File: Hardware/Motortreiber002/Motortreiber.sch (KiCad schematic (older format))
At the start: 17 parts, among them J2 Screw_Terminal_01x04, J3 Screw_Terminal_01x04, U1 DRV8823

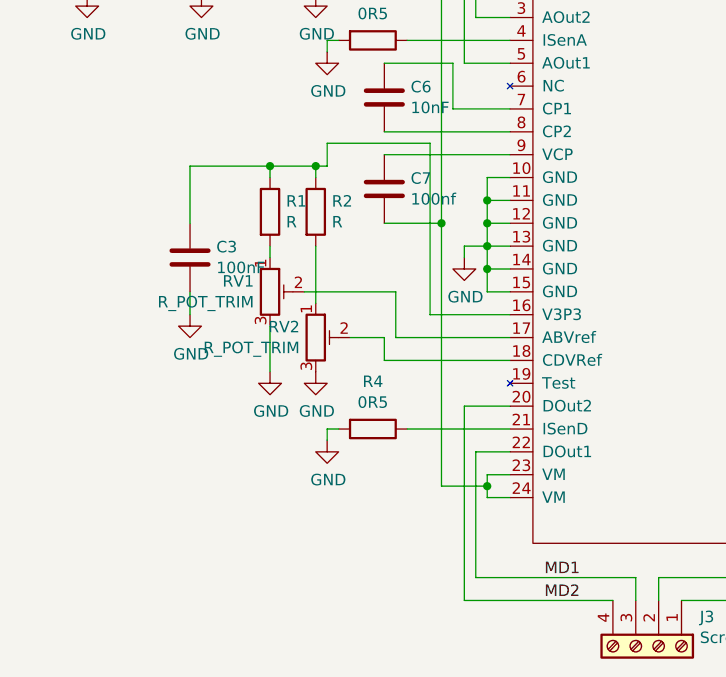
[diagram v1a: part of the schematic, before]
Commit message: 16 Motortreiber 1 ATXMega 128 mit USB USB Anschluss noch nicht fertig
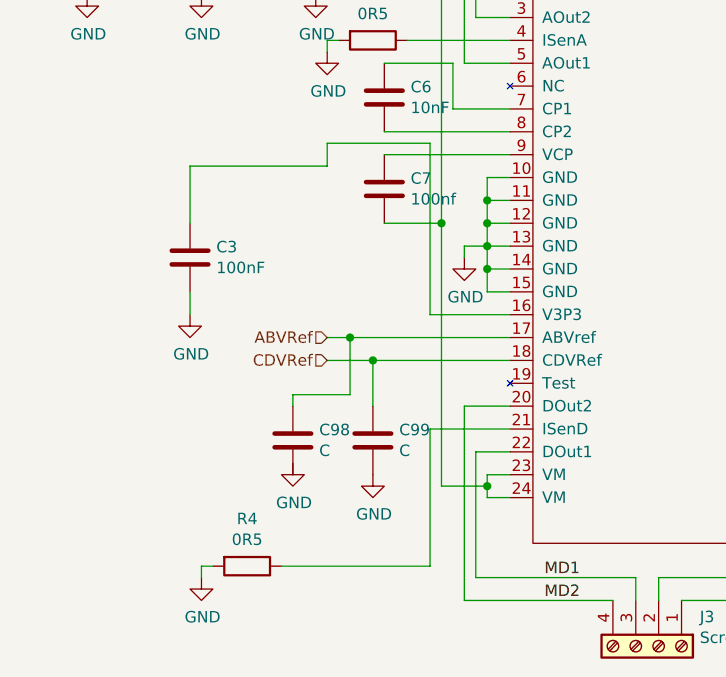
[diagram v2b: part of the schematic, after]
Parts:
- removed R1, R2: R, Resistor_SMD:R_0805_2012Metric_Pad1.15x1.40mm_HandSolder, symbol Device:R
- removed RV1, RV2: R_POT_TRIM, Potentiometer_THT:Potentiometer_Vishay_43_Horizontal, symbol Device:R_POT_TRIM
- added C98, C99: C, symbol Device:C
- renumbered C2 to C20, C3 to C21, C4 to C22, C5 to C23, C6 to C24, C7 to C25, J2 to J8, J3 to J9, R3 to R21, R4 to R22, R5 to R23, R6 to R24, U1 to U4
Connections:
- net GND: now also C99.2
- net ABVRef: now reaches U4.17 (ABVref)
- net ABVRef: now also C98.1
- net CDVRef: now reaches U4.18 (CDVRef)
- net CDVRef: now also C99.1
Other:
- moved on the sheet: R4

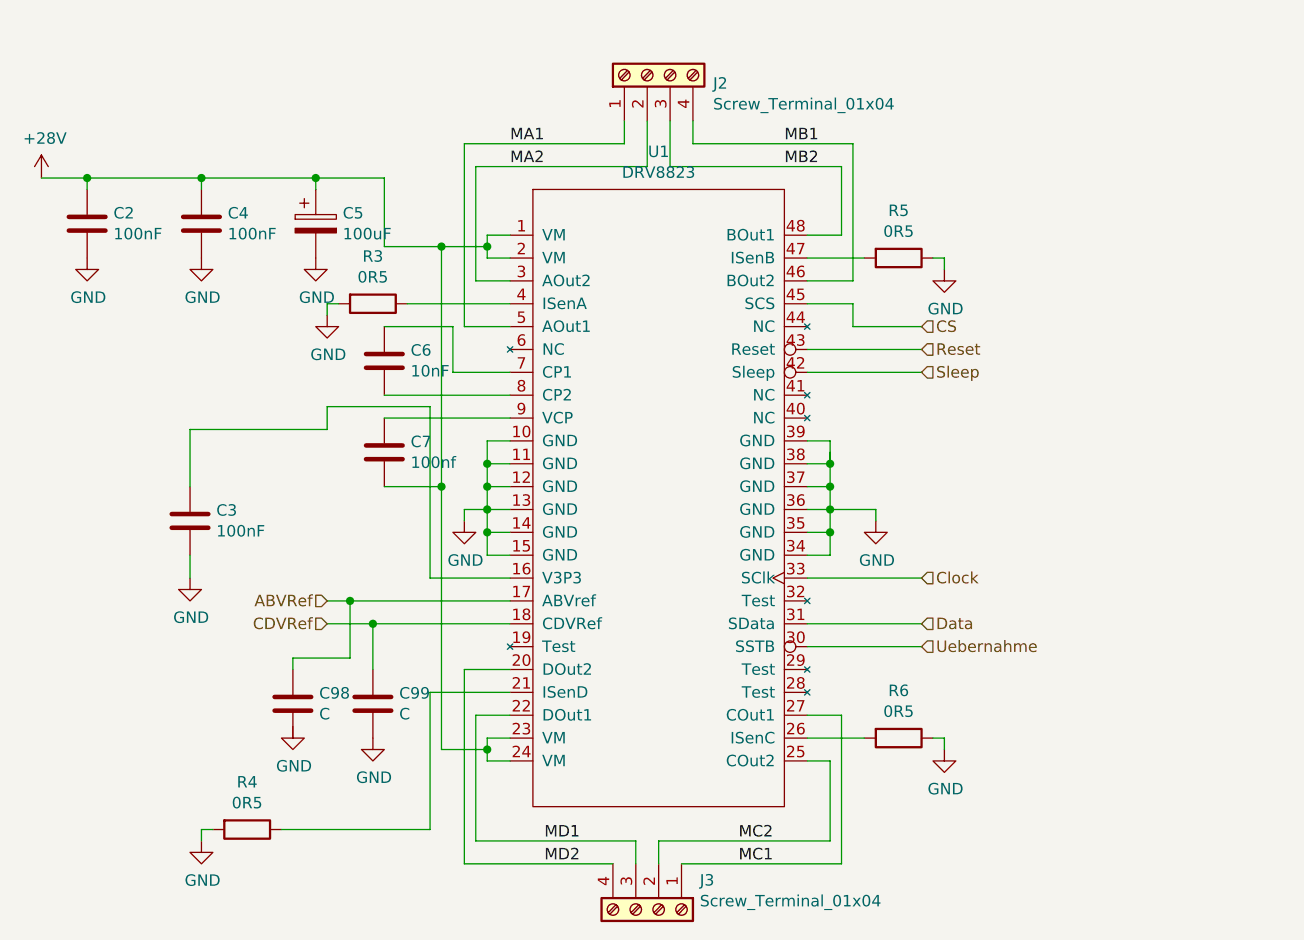
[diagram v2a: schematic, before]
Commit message: Annotation auf Seiten bezogen
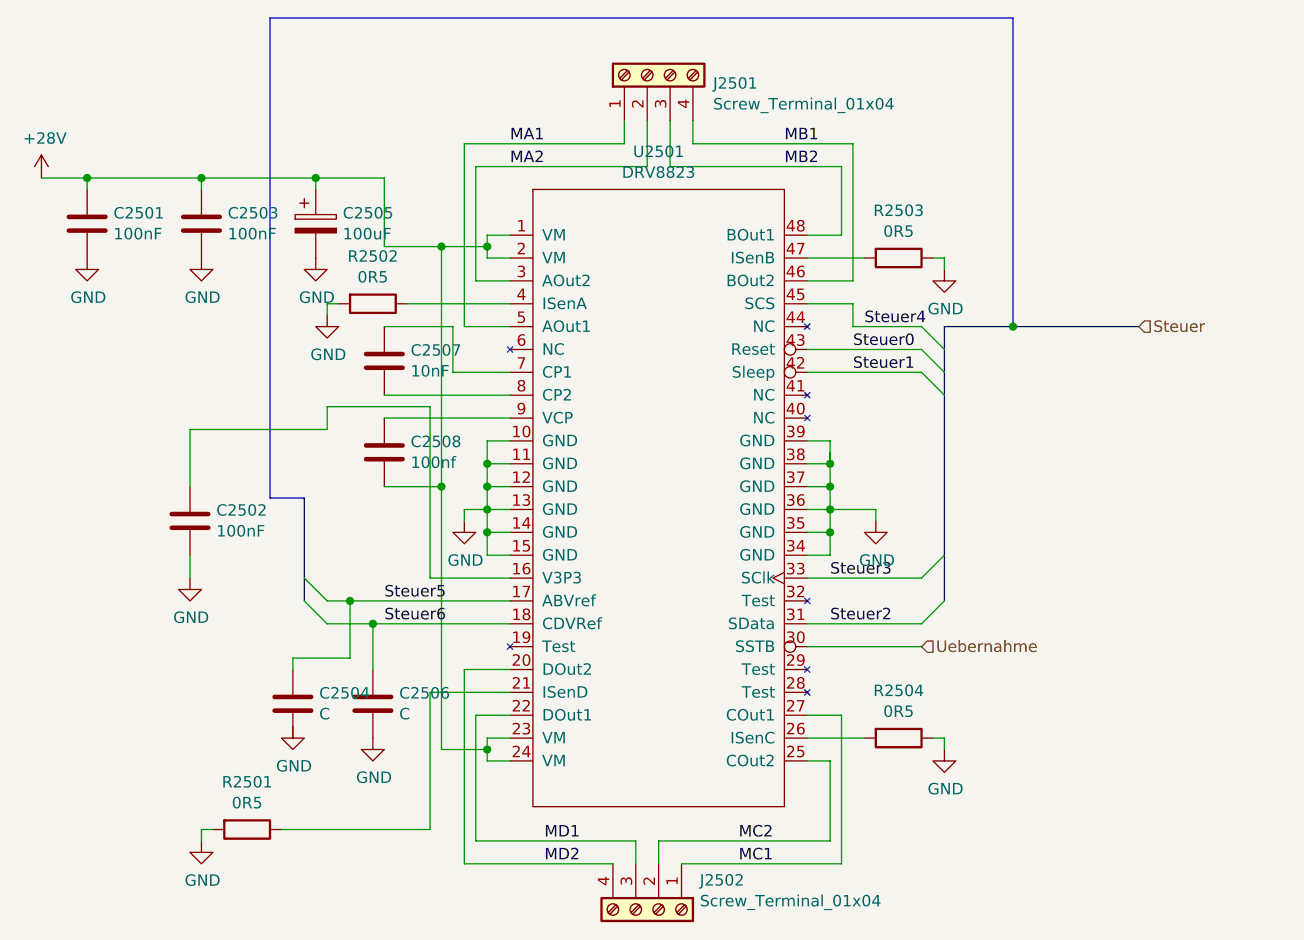
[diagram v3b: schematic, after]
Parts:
- renumbered C20 to C1201, C21 to C1202, C22 to C1203, C23 to C1205, C24 to C1207, C25 to C1208, C98 to C1404, C99 to C1406, J8 to J1201, J9 to J1202, R22 to R1201, R21 to R1202, R23 to R1203, R24 to R1204, U4 to U1201
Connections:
- net ABVRef renamed Steuer5
- net CDVRef renamed Steuer6
- net CS renamed Steuer4
- net Clock renamed Steuer3
- net Data renamed Steuer2
- net Reset renamed Steuer0
- net Sleep renamed Steuer1

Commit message: Erster Motoreiber angefangen routen
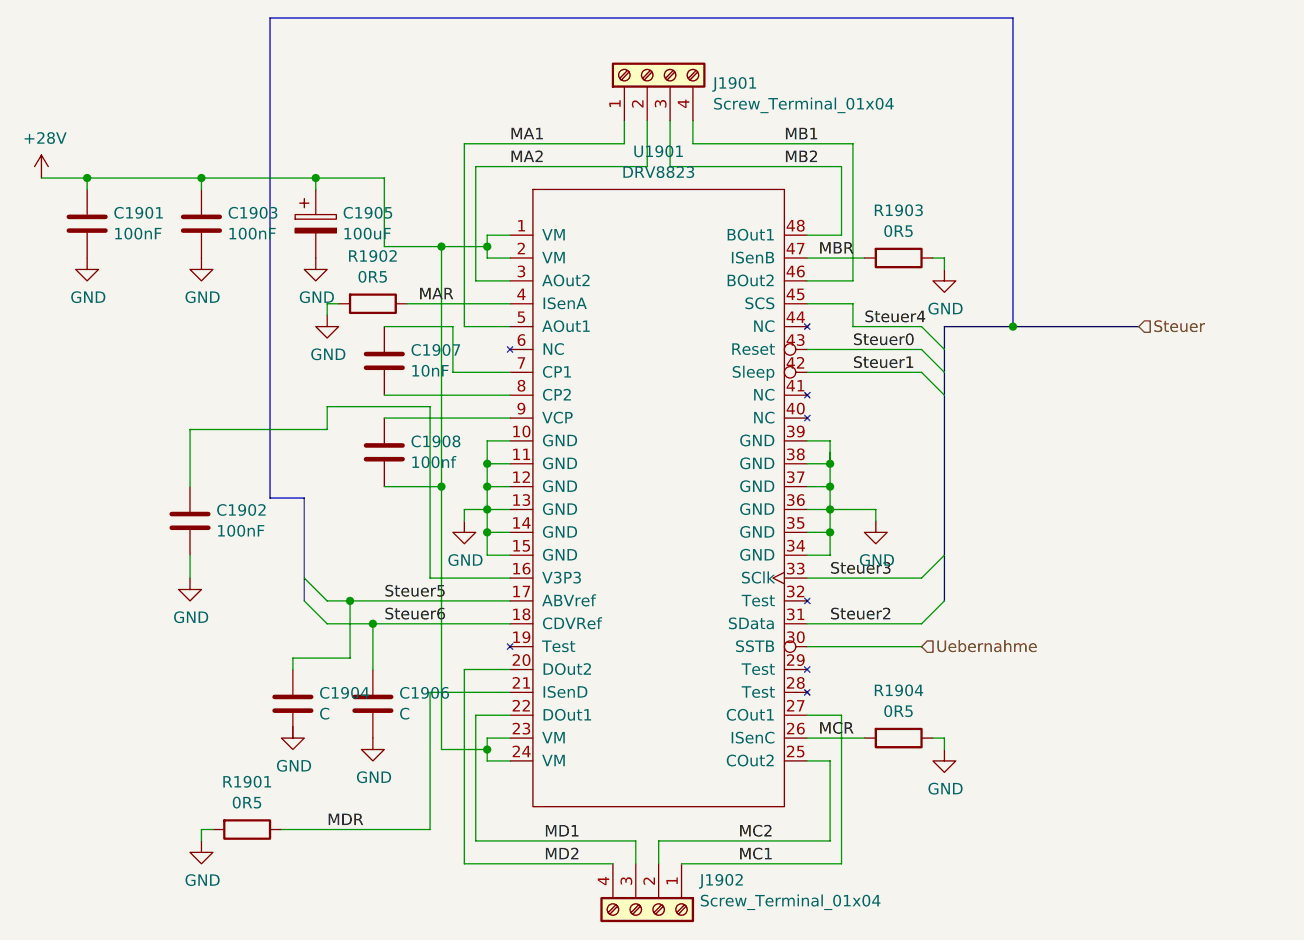
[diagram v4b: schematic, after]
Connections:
- net MDR: now reaches R1201.1, U1201.21 (ISenD)
- net MCR: now reaches R1204.2, U1201.26 (ISenC)
- net MAR: now reaches R1202.1, U1201.4 (ISenA)
- net MBR: now reaches R1203.2, U1201.47 (ISenB)
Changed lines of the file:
@@
 $Descr A4 11693 8268
 encoding utf-8
-Sheet 18 19
+Sheet 8 19
 Title ""
 Date ""
@@
 AR Path="/5CC752B0/5CAFBB89" Ref="#PWR?"  Part="1"
 AR Path="/5CC4B548/5CAFBB89" Ref="#PWR02101"  Part="1"
-F 0 "#PWR02501" H 1950 1900 50  0001 C CNN
+F 0 "#PWR01901" H 1950 1900 50  0001 C CNN
 F 1 "+28V" H 1965 2223 50  0000 C CNN
 F 2 "" H 2200 2100 50  0001 C CNN
@@
 AR Path="/5CC752B0/5CA10EF0" Ref="U?"  Part="1"
 AR Path="/5CC4B548/5CA10EF0" Ref="U2101"  Part="1"
-F 0 "U2501" H 4650 5065 50  0000 C CNN
+F 0 "U1901" H 4650 5065 50  0000 C CNN
 F 1 "DRV8823" H 4650 4974 50  0000 C CNN
 F 2 "Package_SO:TSSOP-48_6.1x12.5mm_P0.5mm" V 4550 3350 50  0001 C CNN
@@
 AR Path="/5CC752B0/5CA5AEA1" Ref="J?"  Part="1"
 AR Path="/5CC4B548/5CA5AEA1" Ref="J2101"  Part="1"
-F 0 "J2501" V 4564 1312 50  0000 R CNN
+F 0 "J1901" V 4564 1312 50  0000 R CNN
 F 1 "Screw_Terminal_01x04" V 4473 1312 50  0000 R CNN
 F 2 "Connector_Phoenix_MC_HighVoltage:PhoenixContact_MCV_1,5_4-G-5.08_1x04_P5.08mm_Vertical" H 4600 1600 50  0001 C CNN
@@
 AR Path="/5CC752B0/5CA5CF1C" Ref="J?"  Part="1"
 AR Path="/5CC4B548/5CA5CF1C" Ref="J2102"  Part="1"
-F 0 "J2502" V 4522 5430 50  0000 L CNN
+F 0 "J1902" V 4522 5430 50  0000 L CNN
 F 1 "Screw_Terminal_01x04" V 4613 5430 50  0000 L CNN
 F 2 "Connector_Phoenix_MC_HighVoltage:PhoenixContact_MCV_1,5_4-G-5.08_1x04_P5.08mm_Vertical" H 4650 5250 50  0001 C CNN
@@
 AR Path="/5CC752B0/5CB597A7" Ref="#PWR?"  Part="1"
 AR Path="/5CC4B548/5CB597A7" Ref="#PWR02111"  Part="1"
-F 0 "#PWR02511" H 5600 3300 50  0001 C CNN
+F 0 "#PWR01911" H 5600 3300 50  0001 C CNN
 F 1 "GND" H 5605 3377 50  0000 C CNN
 F 2 "" H 5600 3550 50  0001 C CNN
@@
 AR Path="/5CC752B0/5CB5E84A" Ref="#PWR?"  Part="1"
 AR Path="/5CC4B548/5CB5E84A" Ref="#PWR02110"  Part="1"
-F 0 "#PWR02510" H 3800 3300 50  0001 C CNN
+F 0 "#PWR01910" H 3800 3300 50  0001 C CNN
 F 1 "GND" H 3805 3377 50  0000 C CNN
 F 2 "" H 3800 3550 50  0001 C CNN
@@
 AR Path="/5CC752B0/5CB640E6" Ref="R?"  Part="1"
 AR Path="/5CC4B548/5CB640E6" Ref="R2102"  Part="1"
-F 0 "R2502" V 3193 2600 50  0000 C CNN
+F 0 "R1902" V 3193 2600 50  0000 C CNN
 F 1 "0R5" V 3284 2600 50  0000 C CNN
 F 2 "Resistor_THT:R_Axial_DIN0411_L9.9mm_D3.6mm_P5.08mm_Vertical" V 3330 2600 50  0001 C CNN
@@
 AR Path="/5CC752B0/5CB64BF2" Ref="R?"  Part="1"
 AR Path="/5CC4B548/5CB64BF2" Ref="R2101"  Part="1"
-F 0 "R2501" V 2643 4900 50  0000 C CNN
+F 0 "R1901" V 2643 4900 50  0000 C CNN
 F 1 "0R5" V 2734 4900 50  0000 C CNN
 F 2 "Resistor_THT:R_Axial_DIN0411_L9.9mm_D3.6mm_P5.08mm_Vertical" V 2780 4900 50  0001 C CNN
@@
 AR Path="/5CC752B0/5CB65616" Ref="R?"  Part="1"
 AR Path="/5CC4B548/5CB65616" Ref="R2104"  Part="1"
-F 0 "R2504" V 5493 4500 50  0000 C CNN
+F 0 "R1904" V 5493 4500 50  0000 C CNN
 F 1 "0R5" V 5584 4500 50  0000 C CNN
 F 2 "Resistor_THT:R_Axial_DIN0411_L9.9mm_D3.6mm_P5.08mm_Vertical" V 5630 4500 50  0001 C CNN
@@
 AR Path="/5CC752B0/5CB65C0C" Ref="R?"  Part="1"
 AR Path="/5CC4B548/5CB65C0C" Ref="R2103"  Part="1"
-F 0 "R2503" V 5493 2400 50  0000 C CNN
+F 0 "R1903" V 5493 2400 50  0000 C CNN
 F 1 "0R5" V 5584 2400 50  0000 C CNN
 F 2 "Resistor_THT:R_Axial_DIN0411_L9.9mm_D3.6mm_P5.08mm_Vertical" V 5630 2400 50  0001 C CNN
@@
 AR Path="/5CC752B0/5CB99402" Ref="#PWR?"  Part="1"
 AR Path="/5CC4B548/5CB99402" Ref="#PWR02108"  Part="1"
-F 0 "#PWR02508" H 3200 2400 50  0001 C CNN
+F 0 "#PWR01908" H 3200 2400 50  0001 C CNN
 F 1 "GND" H 3205 2477 50  0000 C CNN
 F 2 "" H 3200 2650 50  0001 C CNN
@@
 AR Path="/5CC752B0/5CB99CB4" Ref="#PWR?"  Part="1"
 AR Path="/5CC4B548/5CB99CB4" Ref="#PWR02105"  Part="1"
-F 0 "#PWR02505" H 2650 4700 50  0001 C CNN
+F 0 "#PWR01905" H 2650 4700 50  0001 C CNN
 F 1 "GND" H 2655 4777 50  0000 C CNN
 F 2 "" H 2650 4950 50  0001 C CNN
@@
 AR Path="/5CC752B0/5CB99D3F" Ref="#PWR?"  Part="1"
 AR Path="/5CC4B548/5CB99D3F" Ref="#PWR02113"  Part="1"
-F 0 "#PWR02513" H 5900 4300 50  0001 C CNN
+F 0 "#PWR01913" H 5900 4300 50  0001 C CNN
 F 1 "GND" H 5905 4377 50  0000 C CNN
 F 2 "" H 5900 4550 50  0001 C CNN
@@
 AR Path="/5CC752B0/5CB9A10F" Ref="#PWR?"  Part="1"
 AR Path="/5CC4B548/5CB9A10F" Ref="#PWR02112"  Part="1"
-F 0 "#PWR02512" H 5900 2200 50  0001 C CNN
+F 0 "#PWR01912" H 5900 2200 50  0001 C CNN
 F 1 "GND" H 5905 2277 50  0000 C CNN
 F 2 "" H 5900 2450 50  0001 C CNN
@@
 AR Path="/5CC752B0/5CBA36F8" Ref="C?"  Part="1"
 AR Path="/5CC4B548/5CBA36F8" Ref="C2102"  Part="1"
-F 0 "C2502" H 2715 3596 50  0000 L CNN
+F 0 "C1902" H 2715 3596 50  0000 L CNN
 F 1 "100nF" H 2715 3505 50  0000 L CNN
 F 2 "Capacitor_SMD:C_0805_2012Metric_Pad1.15x1.40mm_HandSolder" H 2638 3400 50  0001 C CNN
@@
 AR Path="/5CC752B0/5CBA4977" Ref="#PWR?"  Part="1"
 AR Path="/5CC4B548/5CBA4977" Ref="#PWR02103"  Part="1"
-F 0 "#PWR02503" H 2600 3550 50  0001 C CNN
+F 0 "#PWR01903" H 2600 3550 50  0001 C CNN
 F 1 "GND" H 2605 3627 50  0000 C CNN
 F 2 "" H 2600 3800 50  0001 C CNN
@@
 AR Path="/5CC752B0/5CBD32BF" Ref="C?"  Part="1"
 AR Path="/5CC4B548/5CBD32BF" Ref="C2107"  Part="1"
-F 0 "C2507" H 3565 2896 50  0000 L CNN
+F 0 "C1907" H 3565 2896 50  0000 L CNN
 F 1 "10nF" H 3565 2805 50  0000 L CNN
 F 2 "Capacitor_SMD:C_0805_2012Metric" H 3488 2700 50  0001 C CNN
@@
 AR Path="/5CC752B0/5CBD3B7F" Ref="C?"  Part="1"
 AR Path="/5CC4B548/5CBD3B7F" Ref="C2108"  Part="1"
-F 0 "C2508" H 3565 3296 50  0000 L CNN
+F 0 "C1908" H 3565 3296 50  0000 L CNN
 F 1 "100nf" H 3565 3205 50  0000 L CNN
 F 2 "Capacitor_SMD:C_0805_2012Metric_Pad1.15x1.40mm_HandSolder" H 3488 3100 50  0001 C CNN
@@
 AR Path="/5CC752B0/5CC199C8" Ref="C?"  Part="1"
 AR Path="/5CC4B548/5CC199C8" Ref="C2101"  Part="1"
-F 0 "C2501" H 2265 2296 50  0000 L CNN
+F 0 "C1901" H 2265 2296 50  0000 L CNN
 F 1 "100nF" H 2265 2205 50  0000 L CNN
 F 2 "Capacitor_THT:C_Disc_D8.0mm_W5.0mm_P5.00mm" H 2188 2100 50  0001 C CNN
@@
 AR Path="/5CC752B0/5CC1A57F" Ref="C?"  Part="1"
 AR Path="/5CC4B548/5CC1A57F" Ref="C2103"  Part="1"
-F 0 "C2503" H 2765 2296 50  0000 L CNN
+F 0 "C1903" H 2765 2296 50  0000 L CNN
 F 1 "100nF" H 2765 2205 50  0000 L CNN
 F 2 "Capacitor_THT:C_Disc_D8.0mm_W5.0mm_P5.00mm" H 2688 2100 50  0001 C CNN
@@
 AR Path="/5CC752B0/5CC1B08E" Ref="#PWR?"  Part="1"
 AR Path="/5CC4B548/5CC1B08E" Ref="#PWR02102"  Part="1"
-F 0 "#PWR02502" H 2150 2150 50  0001 C CNN
+F 0 "#PWR01902" H 2150 2150 50  0001 C CNN
 F 1 "GND" H 2155 2227 50  0000 C CNN
 F 2 "" H 2150 2400 50  0001 C CNN
@@
 AR Path="/5CC752B0/5CC1B34B" Ref="#PWR?"  Part="1"
 AR Path="/5CC4B548/5CC1B34B" Ref="#PWR02104"  Part="1"
-F 0 "#PWR02504" H 2650 2150 50  0001 C CNN
+F 0 "#PWR01904" H 2650 2150 50  0001 C CNN
 F 1 "GND" H 2655 2227 50  0000 C CNN
 F 2 "" H 2650 2400 50  0001 C CNN
@@
 AR Path="/5CC752B0/5CC1B722" Ref="C?"  Part="1"
 AR Path="/5CC4B548/5CC1B722" Ref="C2105"  Part="1"
-F 0 "C2505" H 3268 2296 50  0000 L CNN
+F 0 "C1905" H 3268 2296 50  0000 L CNN
 F 1 "100uF" H 3268 2205 50  0000 L CNN
 F 2 "Capacitor_THT:CP_Radial_D8.0mm_P3.50mm" H 3188 2100 50  0001 C CNN
@@
 AR Path="/5CC752B0/5CC1C247" Ref="#PWR?"  Part="1"
 AR Path="/5CC4B548/5CC1C247" Ref="#PWR02107"  Part="1"
-F 0 "#PWR02507" H 3150 2150 50  0001 C CNN
+F 0 "#PWR01907" H 3150 2150 50  0001 C CNN
 F 1 "GND" H 3155 2227 50  0000 C CNN
 F 2 "" H 3150 2400 50  0001 C CNN
@@
 AR Path="/5CC7522D/5CCBF437" Ref="C2206"  Part="1"
 AR Path="/5CC4B548/5CCBF437" Ref="C2106"  Part="1"
-F 0 "C2506" H 3515 4396 50  0000 L CNN
+F 0 "C1906" H 3515 4396 50  0000 L CNN
 F 1 "C" H 3515 4305 50  0000 L CNN
 F 2 "" H 3438 4200 50  0001 C CNN
@@
 AR Path="/5CC7522D/5CCBF8F9" Ref="C2204"  Part="1"
 AR Path="/5CC4B548/5CCBF8F9" Ref="C2104"  Part="1"
-F 0 "C2504" H 3165 4396 50  0000 L CNN
+F 0 "C1904" H 3165 4396 50  0000 L CNN
 F 1 "C" H 3165 4305 50  0000 L CNN
 F 2 "" H 3088 4200 50  0001 C CNN
@@
 AR Path="/5CC7522D/5CCBFD0C" Ref="#PWR02209"  Part="1"
 AR Path="/5CC4B548/5CCBFD0C" Ref="#PWR02109"  Part="1"
-F 0 "#PWR02509" H 3400 4250 50  0001 C CNN
+F 0 "#PWR01909" H 3400 4250 50  0001 C CNN
 F 1 "GND" H 3405 4327 50  0000 C CNN
 F 2 "" H 3400 4500 50  0001 C CNN
@@
 AR Path="/5CC7522D/5CCBFDA5" Ref="#PWR02206"  Part="1"
 AR Path="/5CC4B548/5CCBFDA5" Ref="#PWR02106"  Part="1"
-F 0 "#PWR02506" H 3050 4200 50  0001 C CNN
+F 0 "#PWR01906" H 3050 4200 50  0001 C CNN
 F 1 "GND" H 3055 4277 50  0000 C CNN
 F 2 "" H 3050 4450 50  0001 C CNN
@@
 Text HLabel 6750 2700 2    50   Input ~ 0
 Steuer
+Text HLabel 5800 4100 2    50   Input ~ 0
+Uebernahme
 Wire Bus Line
 	3100 3450 3100 3900
 Wire Bus Line
 	5900 2700 5900 3900
-Text HLabel 5800 4100 2    50   Input ~ 0
-Uebernahme
+Text Label 3600 2600 0    50   ~ 0
+MAR
+Text Label 5350 2400 0    50   ~ 0
+MBR
+Text Label 3200 4900 0    50   ~ 0
+MDR
+Text Label 5350 4500 0    50   ~ 0
+MCR
 $EndSCHEMATC
